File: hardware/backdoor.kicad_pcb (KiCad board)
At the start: 2 copper layers, 49 x 38.2 mm, 30 parts, among them J1 E1, Q1 J201, U1 OP07

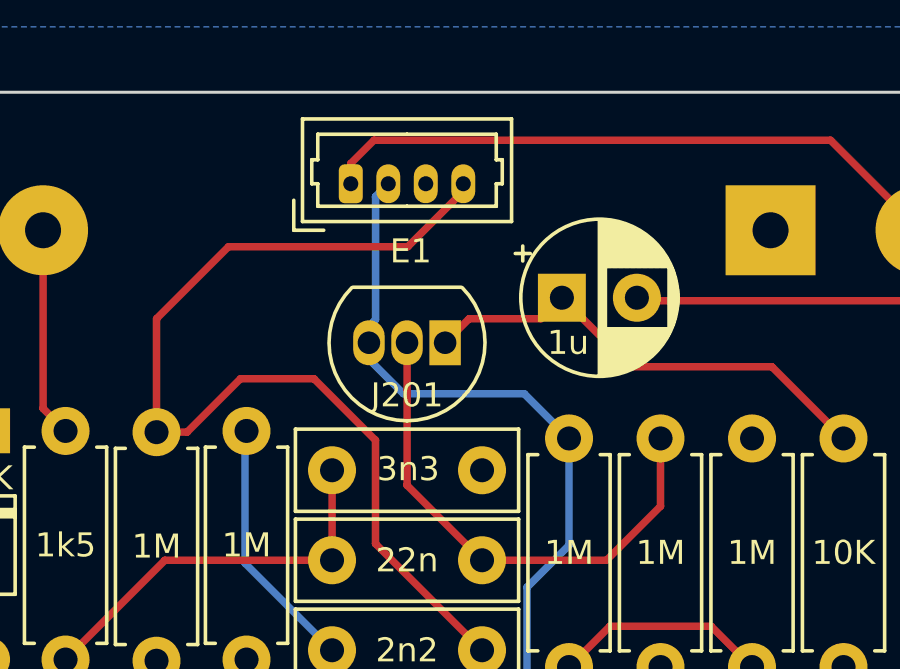
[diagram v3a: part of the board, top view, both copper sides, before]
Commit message: Fix issue identified in v0.02 hardware
 - update schematic to use correct pin for jfet output buffer
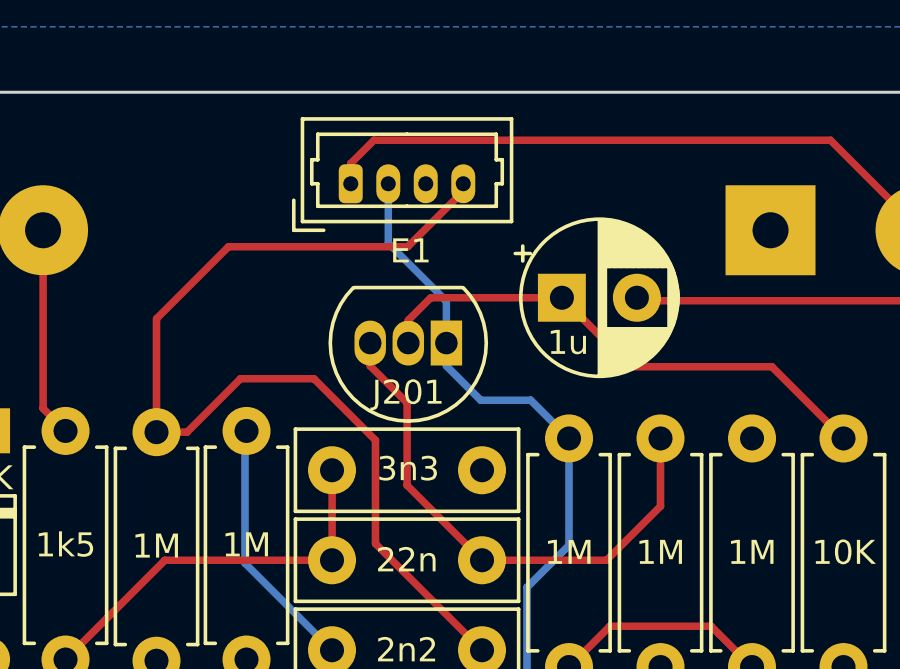
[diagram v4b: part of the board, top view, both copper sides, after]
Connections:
- Q1 pad 1: /Buffer_Out -> /9V0
- Q1 pad 2: /Pre-Buffer -> /Buffer_Out
- Q1 pad 3: /9V0 -> /Pre-Buffer
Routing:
- net /9V0: track 32.0 -> 30.1 mm
- net /Buffer_Out: track 15.8 -> 17.5 mm
